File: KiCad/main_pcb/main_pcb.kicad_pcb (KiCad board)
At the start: 2 copper layers, 69.7 x 75.1 mm, 57 parts, among them J1 Conn_01x06, J2 Conn_01x21, J3 Conn_01x13, J4 Conn_01x07, J5 Conn_01x07, J6 USB_C_Receptacle_USB2.0_14P, J7 Conn_01x01, J8 Conn_01x01, SW1 SW_Push, U1 ATmega2560-16A, U2 TXB0104D, U3 TXB0104D, U4 TXB0104D, U5 CH340C, U6 AMS1117-3.3, Y1 Crystal_GND24

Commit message: feat(schematic): Fixing mistakes
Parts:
- C16: value 100nF -> 10uF

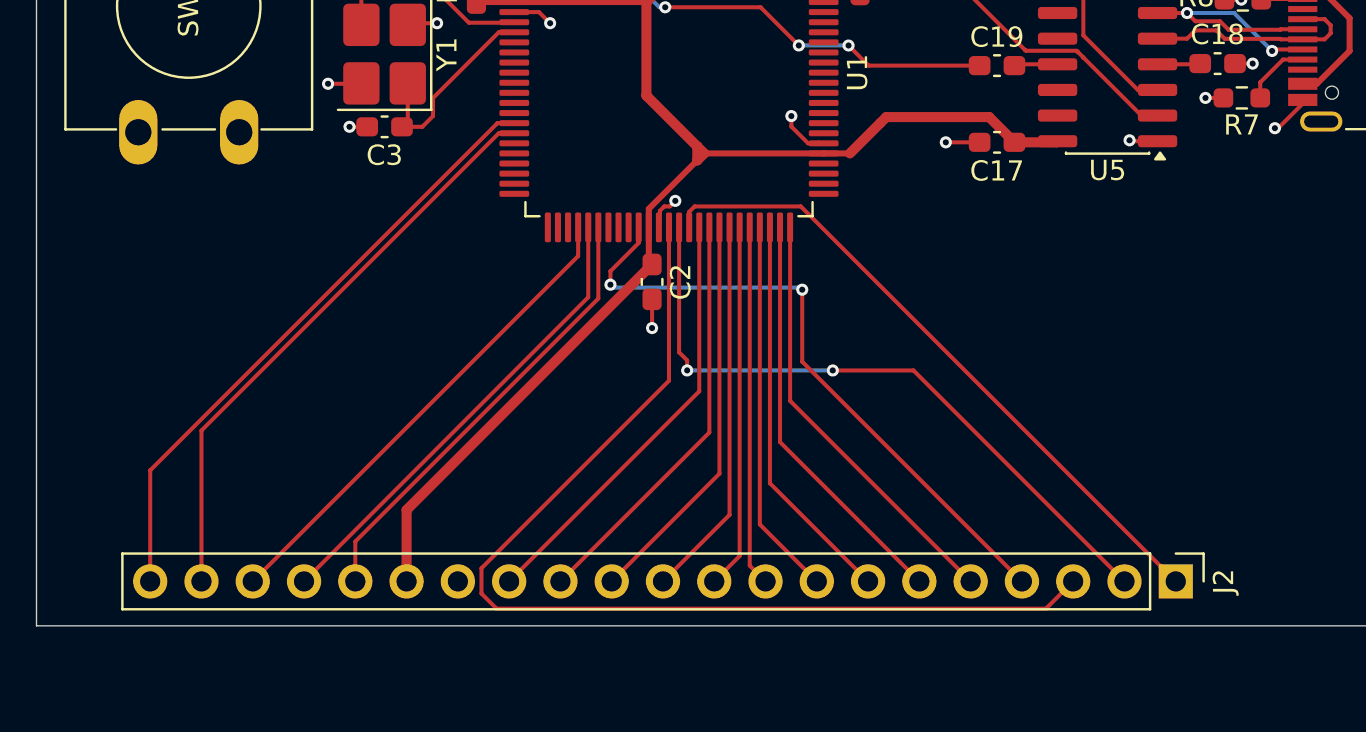
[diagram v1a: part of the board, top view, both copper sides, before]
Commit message: feat(schematic & pcb): Switches to 2 rows header for keyboard connection
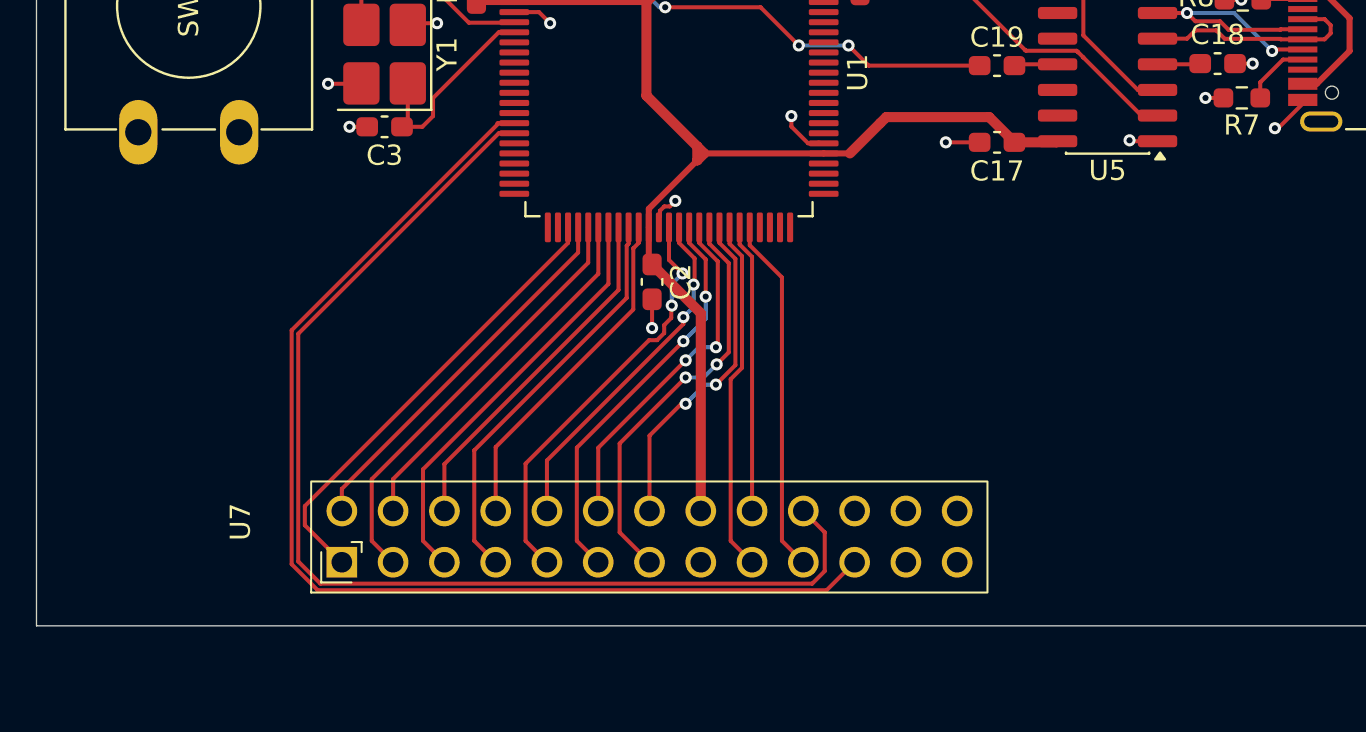
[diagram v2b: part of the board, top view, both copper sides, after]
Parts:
- removed J2: Conn_01x21, Connector_PinHeader_2.54mm:PinHeader_1x21_P2.54mm_Vertical
- added U7: ~, Lilibrary:male_header, F.Cu at (69.0, 131.5)
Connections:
- U1 pad 53: unconnected-(U1-PC0-Pad53) -> /R1
- U1 pad 54: /SDL_SW1 -> /R2
- U1 pad 55: /SDL_SW2 -> /R3
- U1 pad 56: /SDL_SW3 -> /R4
- U1 pad 57: unconnected-(U1-PC4-Pad57) -> /C1
- U1 pad 58: unconnected-(U1-PC5-Pad58) -> /C2
- U1 pad 59: unconnected-(U1-PC6-Pad59) -> /C3
- U1 pad 60: /R4 -> /C4
- U1 pad 63: /R3 -> /C5
- U1 pad 64: /R2 -> /C6
- U1 pad 65: /R1 -> /C7
- U1 pad 66: /C10 -> /C8
- U1 pad 68: /C8 -> /C10
- U1 pad 69: /C7 -> /SDL_SW1
- U1 pad 70: /C6 -> /SDL_SW2
- U1 pad 71: /C5 -> /SDL_SW3
- U1 pad 72: /C4 -> unconnected-(U1-PA6-Pad72)
- U1 pad 73: /C3 -> unconnected-(U1-PA5-Pad73)
- U1 pad 74: /C2 -> unconnected-(U1-PA4-Pad74)
- U1 pad 75: /C1 -> unconnected-(U1-PA3-Pad75)
- U5 pad 2: /USB-C/TXD -> /USB-C/RXD
- U5 pad 3: /USB-C/RXD -> /USB-C/TXD
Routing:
- net /R3: track 52.2 -> 22.0 mm
- net /SDA: track 29.1 -> 56.3 mm
- net /SCL: track 30.7 -> 56.7 mm
- net /R2: track 33.2 -> 18.9 mm, vias 2 -> 0
- net /R4: track 32.0 -> 18.3 mm, vias 2 -> 0
- net /R1: track 32.7 -> 22.7 mm
- net /SDL_SW2: track 23.4 -> 14.3 mm
- net VCC: track 200.0 -> 192.3 mm
- net /SDL_SW1: track 24.2 -> 17.5 mm
- net /C10: track 21.4 -> 16.6 mm, vias 0 -> 2
- net /SDL_SW3: track 22.5 -> 17.7 mm
- net /C5: track 17.9 -> 20.8 mm, vias 0 -> 2
- net /C2: track 20.4 -> 17.6 mm
- net /C8: track 19.7 -> 17.4 mm, vias 0 -> 2
- net /C4: track 18.7 -> 17.0 mm
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
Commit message: feat(pcb): Keeps working on version 2 of main PCB
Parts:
- removed J7, J8: Conn_01x01, Connector_PinHeader_2.54mm:PinHeader_1x01_P2.54mm_Vertical
- added J2: Conn_01x02, Connector_JST:JST_XH_B2B-XH-A_1x02_P2.50mm_Vertical, F.Cu at (164.5, 123.0)
- added TP6: Test Main Screen CS, TestPoint:TestPoint_Pad_D4.0mm, F.Cu at (125.0, 97.2)
- TP1, TP2, TP3, TP4, TP5, TP7: footprint TestPoint:TestPoint_Pad_D1.0mm -> TestPoint:TestPoint_Pad_D4.0mm
- moved R3 61.0 mm to (142.1, 136.1), turned to 180 degrees
- moved R7 58.7 mm to (166.7, 143.3), turned to 0 degrees
- moved D2 58.3 mm to (135.6, 136.1), turned to 0 degrees
- moved R2 57.9 mm to (142.1, 133.1), turned to 180 degrees
- moved SW1 57.5 mm to (116.0, 132.0), turned to 0 degrees
- moved C17 56.3 mm to (158.8, 132.2), turned to -90 degrees
- moved D1 55.0 mm to (135.6, 133.1), turned to 0 degrees
- moved C14 54.1 mm to (159.0, 122.6), turned to -90 degrees
- moved J6 53.2 mm to (170.2, 135.6)
- moved U5 51.7 mm to (153.5, 138.3), turned to 0 degrees
- moved R8 51.5 mm to (162.0, 132.5), turned to 90 degrees
- moved C16 50.5 mm to (156.4, 122.6), turned to -90 degrees
- moved C15 46.9 mm to (153.7, 122.6), turned to -90 degrees
- moved C20 46.2 mm to (149.5, 120.9), turned to -90 degrees
- moved R9 45.8 mm to (155.8, 127.9), turned to -90 degrees
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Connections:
- net Net-(J3-Pin_10) renamed /Screens/SD_CS-3V3
- net Net-(J3-Pin_3) renamed /Screens/MAIN_SCREEN_CS-3V3
- net Net-(J3-Pin_4) renamed /Screens/MAIN_SCREEN_RST-3V3
- net Net-(J3-Pin_5) renamed /Screens/DC-3V3
- net Net-(J3-Pin_8) renamed /Screens/MAIN_SCREEN_BL-3V3
- net Net-(J4-Pin_6) renamed /Screens/LEFT_EYE_CS-3V3
- net Net-(J5-Pin_6) renamed /Screens/RIGHT_EYE_CS-3V3
- D5 pad 1: Net-(D5-K) -> GND
- D5 pad 2: VCC -> Net-(D5-A)
- J4 pad 7: Net-(J4-Pin_7) -> /Screens/EYES_RST-3V3
- J5 pad 7: Net-(J4-Pin_7) -> /Screens/EYES_RST-3V3
- R9 pad 1: Net-(D5-K) -> VCC
- R9 pad 2: GND -> Net-(D5-A)
- U4 pad 10: unconnected-(U4-B4-Pad10) -> /Screens/Eyes_RST
- U4 pad 12: /Screens/Eyes_RST -> unconnected-(U4-B2-Pad12)
- U4 pad 3: Net-(J4-Pin_7) -> unconnected-(U4-A2-Pad3)
- U4 pad 5: unconnected-(U4-A4-Pad5) -> /Screens/EYES_RST-3V3
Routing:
- net VCC: track 192.3 -> 114.7 mm, vias 2 -> 0
- net /SDA: track 56.3 -> 0.00 mm
- net /SCL: track 56.7 -> 0.84 mm
- net /Screens/DC-3V3: track 50.1 -> 0.00 mm
- net Net-(J4-Pin_7): track 40.2 -> 0.00 mm, vias 2 -> 0
- net /Screens/RIGHT_EYE_CS-3V3: track 36.1 -> 0.00 mm, vias 2 -> 0
- net /Screens/MOSI_3V3: track 49.1 -> 14.4 mm
- net /USB-C/D+: track 11.0 -> 42.5 mm
- net GND: track 58.6 -> 86.2 mm, vias 40 -> 31
- net /USB-C/D-: track 14.1 -> 41.5 mm, vias 2 -> 0
- net /Screens/DC: track 26.8 -> 0.00 mm, vias 2 -> 0
- net /Screens/SCK_3V3: track 43.1 -> 17.3 mm
- net /Screens/Left_Eye_CS: track 25.3 -> 0.00 mm
- net Net-(U5-~{DTR}): track 2.16 -> 25.6 mm
- net /Screens/Right_Eye_CS: track 23.4 -> 0.00 mm
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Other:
- board size 69.7 x 75.1 mm -> 130 x 100 mm
- board text added: "3V3"
- board text added: "5V"
- board text added: "D/C"
- board text added: "EYES RST"
- board text added: "GND"
- board text added: "LEFT EYE"
- board text added: "LEFT EYE CS"
- board text added: "MAIN SCREEN"
- board text added: "MAIN SCREEN BL"
- board text added: "MAIN SCREEN CS"
- board text added: "MAIN SCREEN RST"
- board text added: "MISO"
- board text added: "MOSI"
- board text added: "R2 R4 C2 C4 C6 C8 C10 VCC SL2 SDA X X X R1 R3 C1 C3 C5 C7 C9 GND SL1 SL3 SCK X X"
- board text added: "RIGHT EYE"
- board text added: "RIGHT EYE CS"
- board text added: "SCK"
- board text added: "SD CS"
- board text added: "SPI"
- board text added: "USB-C RST"

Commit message: feat(PCB): Continues work on PCB v2.
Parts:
- TP1, TP2, TP3, TP4, TP5, TP6, TP7: footprint TestPoint:TestPoint_Pad_D4.0mm -> TestPoint:TestPoint_Pad_D2.0mm
- moved TP5 82.9 mm to (54.4, 47.8)
- moved TP4 72.7 mm to (80.3, 47.8)
- moved TP7 55.3 mm to (136.2, 49.0)
- moved TP3 51.1 mm to (111.2, 52.8)
- moved TP6 44.8 mm to (136.2, 53.8)
- moved C11 32.9 mm to (73.2, 74.1)
- moved C12 32.9 mm to (73.2, 78.4)
- moved C2 23.7 mm to (101.2, 99.4), turned to 90 degrees
- moved C5 22.3 mm to (100.2, 74.4)
- moved C6 22.2 mm to (100.2, 78.6)
- moved R6 4.56 mm to (110.0, 69.2)
- moved U2 4.37 mm to (93.1, 76.5)
- moved U4 2.97 mm to (65.8, 76.5)
- moved C7 2.00 mm to (127.5, 74.5)
- moved C8 2.00 mm to (127.5, 78.4)
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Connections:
- TP3 pad 1: /Screens/SD_CS -> /Screens/SD_CS-3V3
- TP4 pad 1: /Screens/Right_Eye_CS -> /Screens/RIGHT_EYE_CS-3V3
- TP5 pad 1: /Screens/Left_Eye_CS -> /Screens/LEFT_EYE_CS-3V3
- TP6 pad 1: /Screens/Main_Screen_CS -> /Screens/MAIN_SCREEN_CS-3V3
- TP7 pad 1: /Screens/DC -> /Screens/DC-3V3
- U1 pad 12: /Screens/Main_Screen_CS -> unconnected-(U1-PH0-Pad12)
- U1 pad 13: /Screens/Main_Screen_RST -> unconnected-(U1-PH1-Pad13)
- U1 pad 14: /Screens/Main_Screen_LED/BL -> unconnected-(U1-PH2-Pad14)
- U1 pad 15: unconnected-(U1-PH3-Pad15) -> /Screens/Right_Eye_CS
- U1 pad 16: unconnected-(U1-PH4-Pad16) -> /Screens/Left_Eye_CS
- U1 pad 17: /Screens/SD_CS -> /Screens/Eyes_RST
- U1 pad 6: unconnected-(U1-PE4-Pad6) -> /Screens/Main_Screen_CS
- U1 pad 7: /Screens/Left_Eye_CS -> /Screens/Main_Screen_RST
- U1 pad 8: /Screens/Eyes_RST -> /Screens/Main_Screen_LED/BL
- U1 pad 9: /Screens/Right_Eye_CS -> /Screens/SD_CS
- U2 pad 10: /Screens/DC -> /MISO
- U2 pad 12: /MISO -> /SCK
- U2 pad 13: /SCK -> /Screens/DC
- U4 pad 10: /Screens/Eyes_RST -> unconnected-(U4-B4-Pad10)
- U4 pad 11: /Screens/Right_Eye_CS -> /Screens/Eyes_RST
- U4 pad 12: unconnected-(U4-B2-Pad12) -> /Screens/Left_Eye_CS
- U4 pad 13: /Screens/Left_Eye_CS -> /Screens/Right_Eye_CS
- U4 pad 2: /Screens/LEFT_EYE_CS-3V3 -> /Screens/RIGHT_EYE_CS-3V3
- U4 pad 3: unconnected-(U4-A2-Pad3) -> /Screens/LEFT_EYE_CS-3V3
- U4 pad 4: /Screens/RIGHT_EYE_CS-3V3 -> /Screens/EYES_RST-3V3
- U4 pad 5: /Screens/EYES_RST-3V3 -> unconnected-(U4-A4-Pad5)
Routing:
- net VCC: track 114.7 -> 333.5 mm
- net 3V3: track 103.0 -> 242.0 mm
- net /Screens/DC-3V3: track 0.00 -> 113.2 mm, vias 0 -> 6
- net /Screens/MOSI_3V3: track 14.4 -> 92.8 mm, vias 0 -> 8
- net /USB-C/TXD: track 8.15 -> 80.4 mm, vias 0 -> 2
- net /Screens/SCK_3V3: track 17.3 -> 87.8 mm, vias 0 -> 2
- net /USB-C/RXD: track 8.87 -> 76.1 mm, vias 0 -> 2
- net /Screens/Main_Screen_CS: track 0.00 -> 40.8 mm, vias 0 -> 2
- net /Screens/Main_Screen_RST: track 0.00 -> 40.3 mm, vias 0 -> 2
- net /Screens/Main_Screen_LED/BL: track 0.00 -> 39.3 mm, vias 0 -> 2
- net /Screens/SD_CS: track 0.00 -> 38.7 mm, vias 0 -> 2
- net /Screens/Eyes_RST: track 0.00 -> 36.1 mm, vias 0 -> 2
- net /Screens/Left_Eye_CS: track 0.00 -> 35.7 mm, vias 0 -> 2
- net GND: track 86.2 -> 120.8 mm, vias 31 -> 35
- net /Screens/Right_Eye_CS: track 0.00 -> 34.6 mm, vias 0 -> 2
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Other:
- board text added: "SD CARD"

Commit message: feat(PCB): Continues work
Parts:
- D/C TP: renamed from TP7
- LEFT EYE CS TP: renamed from TP5
- MAIN SCREEN CS TP: renamed from TP6
- RIGHT EYE CS TP: renamed from TP4
- SD CS TP: renamed from TP3
- moved MISO 43.5 mm to (80.5, 77.0)
- moved MOSI 42.9 mm to (80.2, 72.8)
- moved C18 39.7 mm to (105.6, 139.5)
- moved C17 36.5 mm to (122.2, 132.6)
- moved R2 36.5 mm to (105.6, 133.5)
- moved R3 36.5 mm to (105.6, 136.5)
- moved U5 36.5 mm to (117.0, 138.7)
- moved D1 36.5 mm to (99.1, 133.5)
- moved D2 36.5 mm to (99.1, 136.5)
- moved U6 31.8 mm to (137.6, 92.8), turned to 90 degrees
- moved J2 29.3 mm to (139.8, 138.8), turned to -90 degrees
- moved C21 29.3 mm to (136.9, 85.0)
- moved C16 28.8 mm to (129.4, 132.9)
- moved C14 28.8 mm to (132.1, 132.9)
- moved C15 28.8 mm to (126.8, 132.9)
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- renumbered TP2 to MISO, TP1 to MOSI
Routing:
- net /SCL: track 0.84 -> 88.8 mm, vias 0 -> 2
- net /SDA: track 0.00 -> 87.9 mm, vias 0 -> 2
- net /USB-C/D+: track 21.2 -> 62.7 mm
- net /USB-C/D-: track 20.0 -> 59.2 mm, vias 0 -> 2
- net /SDL_SW3: track 0.00 -> 35.1 mm
- net 3V3: track 242.0 -> 207.4 mm
- net /SDL_SW1: track 0.00 -> 34.1 mm
- net /SDL_SW2: track 0.00 -> 32.5 mm, vias 0 -> 1
- net /USB-C/RXD: track 76.1 -> 58.7 mm
- net /MOSI: track 56.6 -> 73.8 mm, vias 4 -> 5
- net /USB-C/USB-C_RST: track 88.2 -> 71.9 mm
- net /USB-C/TXD: track 80.4 -> 64.2 mm
- net /USB-C/VBUS: track 21.0 -> 35.5 mm
- net /MISO: track 56.2 -> 68.2 mm
- net GND: track 120.8 -> 109.6 mm, vias 35 -> 33
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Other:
- outline, holes or cut-outs redrawn
- board text added: "POWER"
- board text added: "RX"
- board text added: "TX"

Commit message: feat(PCB): Continues work
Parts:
- renumbered C10 to C1, C8 to C10, C4 to C11, C3 to C12, C2 to C13, C1 to C14, C20 to C15, C18 to C16, C14 to C17, C15 to C18, C16 to C19, C12 to C2, C17 to C20, C19 to C21, C11 to C3, C5 to C4, C6 to C5, C13 to C6, C21 to C7, C9 to C8, C7 to C9, D3 to D1, D4 to D2, D2 to D3, D1 to D4, J4 to J1, J5 to J2, J1 to J4, J2 to J5, R6 to R1, R4 to R2, R1 to R3, R5 to R4, R2 to R5, R3 to R6, R8 to R7, R9 to R8, R7 to R9, U4 to U1, U1 to U4, U6 to U5, U7 to U6, U5 to U7
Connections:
- U6 pad 1: /R1 -> /R2
- U6 pad 10: /C6 -> /C5
- U6 pad 11: /C7 -> /C8
- U6 pad 12: /C8 -> /C7
- U6 pad 13: /C9 -> /C10
- U6 pad 14: /C10 -> /C9
- U6 pad 17: /SDL_SW1 -> /SDL_SW2
- U6 pad 18: /SDL_SW2 -> /SDL_SW1
- U6 pad 19: /SDL_SW3 -> /SDA
- U6 pad 2: /R2 -> /R1
- U6 pad 20: /SDA -> /SDL_SW3
- U6 pad 21: /SCL -> unconnected-(U7-SCL-Pad21)
- U6 pad 22: unconnected-(U7-extra-Pad22) -> /SCL
- U6 pad 3: /R3 -> /R4
- U6 pad 4: /R4 -> /R3
- U6 pad 5: /C1 -> /C2
- U6 pad 6: /C2 -> /C1
- U6 pad 7: /C3 -> /C4
- U6 pad 8: /C4 -> /C3
- U6 pad 9: /C5 -> /C6
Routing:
- net VCC: track 333.0 -> 398.0 mm
- net /R2: track 0.00 -> 46.7 mm
- net /R4: track 0.00 -> 45.2 mm
- net /R1: track 0.00 -> 44.3 mm
- net /C2: track 0.00 -> 43.6 mm
- net /R3: track 0.00 -> 42.7 mm
- net /C4: track 0.00 -> 42.3 mm
- net /C6: track 0.00 -> 41.5 mm
- net /C1: track 0.00 -> 41.0 mm
- net /C8: track 0.00 -> 40.0 mm
- net /C3: track 0.00 -> 39.7 mm
- net /C5: track 0.00 -> 39.1 mm
- net /C10: track 0.00 -> 38.5 mm
- net /C7: track 0.00 -> 37.6 mm
- net /C9: track 0.00 -> 36.0 mm
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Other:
- board text added: "R1 R3 C1 C3 C5 C7 C9 GND SL1 SL3 SCK X X R2 R4 C2 C4 C6 C8 C10 VCC SL2 SDA X X X"
- board text removed: "R2 R4 C2 C4 C6 C8 C10 VCC SL2 SDA X X X R1 R3 C1 C3 C5 C7 C9 GND SL1 SL3 SCK X X"
